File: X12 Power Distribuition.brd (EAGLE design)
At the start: 152.4 x 76.2 mm, 47 parts, among them Q1 SPB80P06P, Y1 ECS-80-S-4X

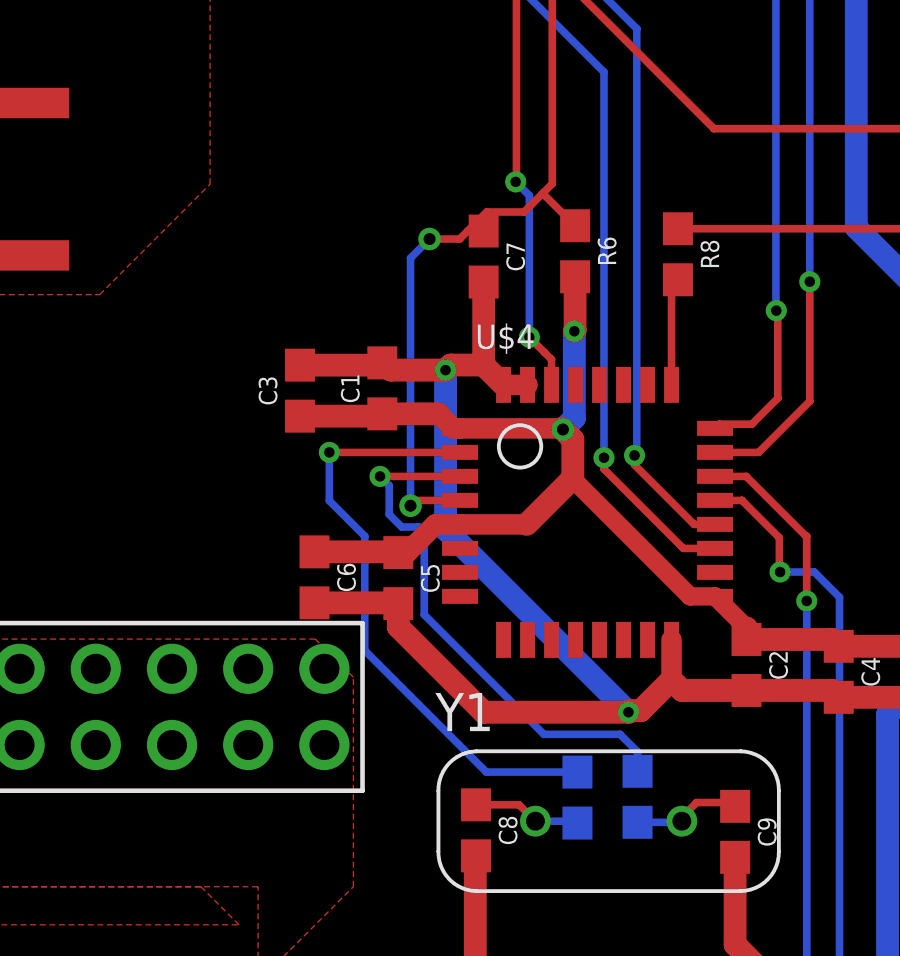
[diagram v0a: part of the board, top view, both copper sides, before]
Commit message: Matched Impedances around crystal
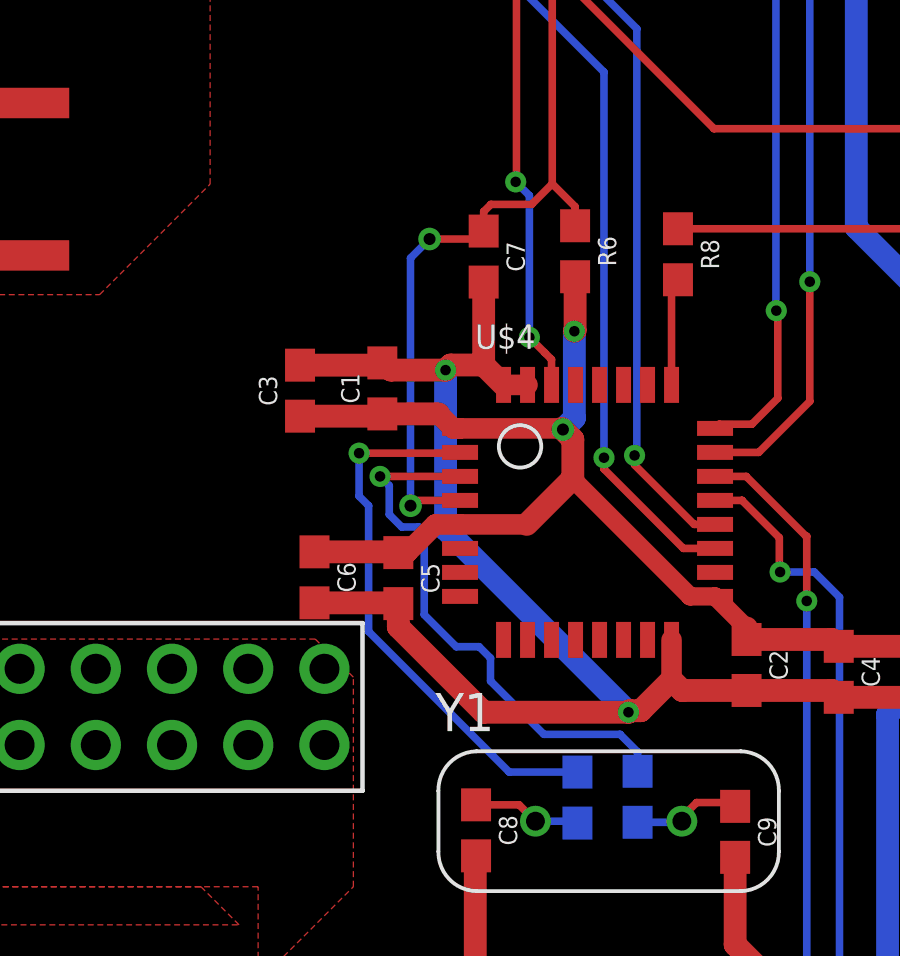
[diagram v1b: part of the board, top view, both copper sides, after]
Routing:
- net OSC_IN: track 20.2 -> 18.4 mm
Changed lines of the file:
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@@
 <wire x1="147.4216" y1="57.652" x2="136.4802" y2="57.652" width="0.254" layer="1"/>
 <wire x1="136.4802" y1="57.652" x2="131.0894" y2="63.0428" width="0.254" layer="1"/>
-<wire x1="131.8514" y1="54.4186" x2="130.7719" y2="55.4981" width="0.254" layer="1"/>
-<wire x1="131.0894" y1="55.8156" x2="130.7719" y2="55.4981" width="0.254" layer="1"/>
-<wire x1="130.1496" y1="54.8758" x2="128.905" y2="54.8758" width="0.254" layer="1"/>
-<wire x1="128.8034" y1="54.2408" x2="128.27" y2="54.2408" width="0.254" layer="1"/>
+<wire x1="131.8514" y1="54.4186" x2="131.8514" y2="55.0536" width="0.254" layer="1"/>
+<wire x1="131.8514" y1="55.0536" x2="131.0894" y2="55.8156" width="0.254" layer="1"/>
 <wire x1="128.016" y1="45.2624" x2="126.5424" y2="45.2624" width="0.254" layer="1"/>
 <wire x1="126.5424" y1="45.2624" x2="126.365" y2="45.085" width="0.254" layer="1"/>
@@
 <wire x1="126.365" y1="53.34" x2="127" y2="53.975" width="0.254" layer="16"/>
 <via x="127" y="53.975" extent="1-16" drill="0.4"/>
-<wire x1="127" y1="53.975" x2="128.0042" y2="53.975" width="0.254" layer="1"/>
-<wire x1="128.27" y1="54.2408" x2="128.905" y2="54.8758" width="0.254" layer="1"/>
-<wire x1="130.7719" y1="55.4981" x2="130.1496" y2="54.8758" width="0.254" layer="1"/>
-<wire x1="128.0042" y1="53.975" x2="128.27" y2="54.2408" width="0.254" layer="1"/>
+<wire x1="130.4036" y1="55.1298" x2="131.0894" y2="55.8156" width="0.254" layer="1"/>
+<wire x1="128.5376" y1="53.975" x2="128.8034" y2="54.2408" width="0.254" layer="1"/>
+<wire x1="127" y1="53.975" x2="128.5376" y2="53.975" width="0.254" layer="1"/>
+<wire x1="128.8034" y1="54.2408" x2="128.8034" y2="54.8894" width="0.254" layer="1"/>
+<wire x1="129.0438" y1="55.1298" x2="130.4036" y2="55.1298" width="0.254" layer="1"/>
+<wire x1="128.8034" y1="54.8894" x2="129.0438" y2="55.1298" width="0.254" layer="1"/>
 </signal>
 <signal name="SWDIO">
@@
 <contactref element="U$4" pad="PF0-OSC_IN"/>
 <contactref element="R7" pad="2"/>
-<wire x1="128.016" y1="46.8624" x2="123.6602" y2="46.8624" width="0.254" layer="1"/>
-<via x="123.6602" y="46.8624" extent="1-16" drill="0.35"/>
-<wire x1="131.9276" y1="36.2068" x2="128.8932" y2="36.2068" width="0.254" layer="16"/>
-<wire x1="123.6602" y1="45.2498" x2="123.6602" y2="46.8624" width="0.254" layer="16"/>
-<wire x1="128.8932" y1="36.2068" x2="124.841" y2="40.259" width="0.254" layer="16"/>
-<wire x1="124.841" y1="40.259" x2="124.841" y2="44.069" width="0.254" layer="16"/>
-<wire x1="124.841" y1="44.069" x2="123.6602" y2="45.2498" width="0.254" layer="16"/>
+<wire x1="128.016" y1="46.8624" x2="127.9906" y2="46.837" width="0.254" layer="1"/>
+<wire x1="127.9906" y1="46.837" x2="124.6508" y2="46.837" width="0.254" layer="1"/>
+<via x="124.6508" y="46.837" extent="1-16" drill="0.35"/>
+<wire x1="131.9276" y1="36.2068" x2="129.6552" y2="36.2068" width="0.254" layer="16"/>
+<wire x1="129.6552" y1="36.2068" x2="124.968" y2="40.894" width="0.254" layer="16"/>
+<wire x1="124.968" y1="40.894" x2="124.968" y2="45.085" width="0.254" layer="16"/>
+<wire x1="124.968" y1="45.085" x2="124.6508" y2="45.4022" width="0.254" layer="16"/>
+<wire x1="124.6508" y1="46.837" x2="124.6508" y2="45.4022" width="0.254" layer="16"/>
 </signal>
 <signal name="OSC_OUT">
@@
 <wire x1="125.657" y1="44.79173125" x2="125.657" y2="45.7548" width="0.254" layer="16"/>
 <wire x1="133.35" y1="37.465" x2="130.81" y2="37.465" width="0.254" layer="16"/>
-<wire x1="130.81" y1="37.465" x2="126.8222" y2="41.4528" width="0.254" layer="16"/>
 <wire x1="126.8222" y1="41.4528" x2="126.8222" y2="44.196" width="0.254" layer="16"/>
+<wire x1="129.032" y1="39.243" x2="129.032" y2="40.005" width="0.254" layer="16"/>
+<wire x1="129.032" y1="40.005" x2="128.651" y2="40.386" width="0.254" layer="16"/>
+<wire x1="127.889" y1="40.386" x2="126.8222" y2="41.4528" width="0.254" layer="16"/>
+<wire x1="130.81" y1="37.465" x2="129.032" y2="39.243" width="0.254" layer="16"/>
+<wire x1="128.651" y1="40.386" x2="127.889" y2="40.386" width="0.254" layer="16"/>
 </signal>
 <signal name="N$6">

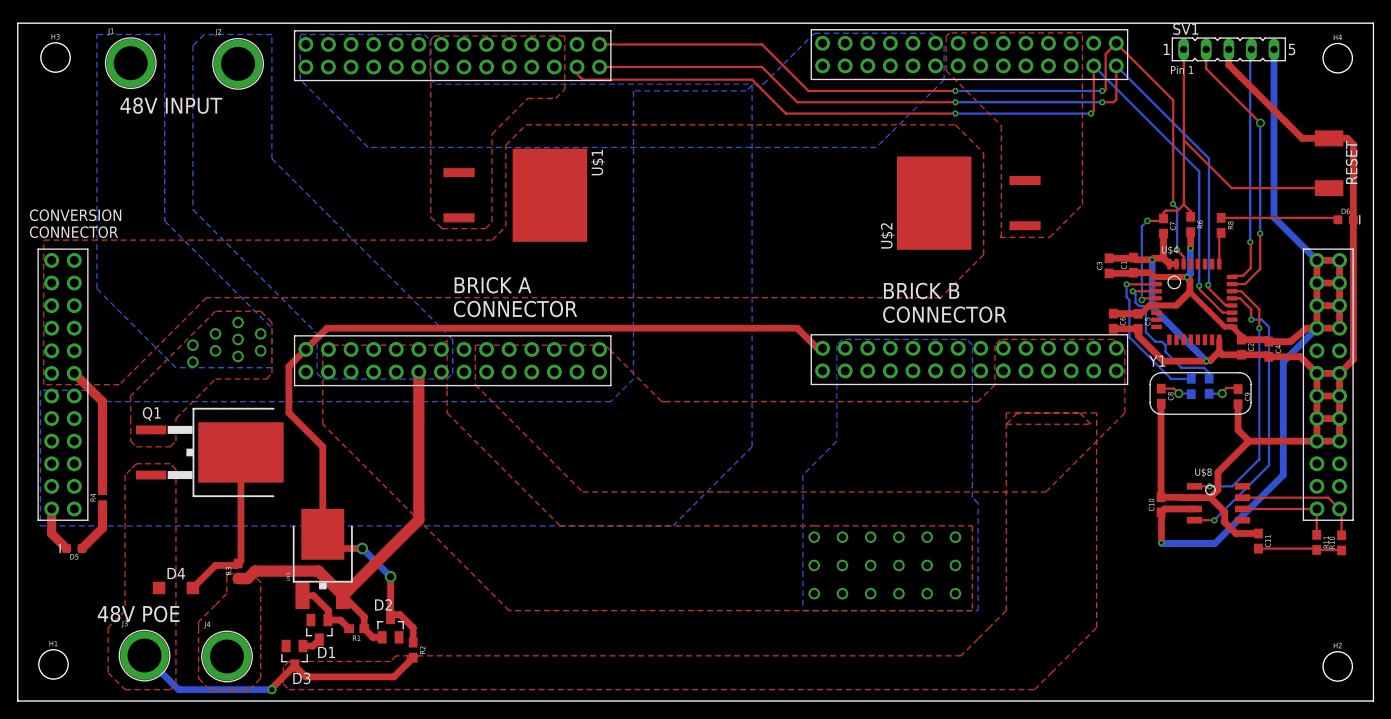
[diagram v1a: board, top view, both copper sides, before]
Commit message: Moved Crystal. Small Fixes
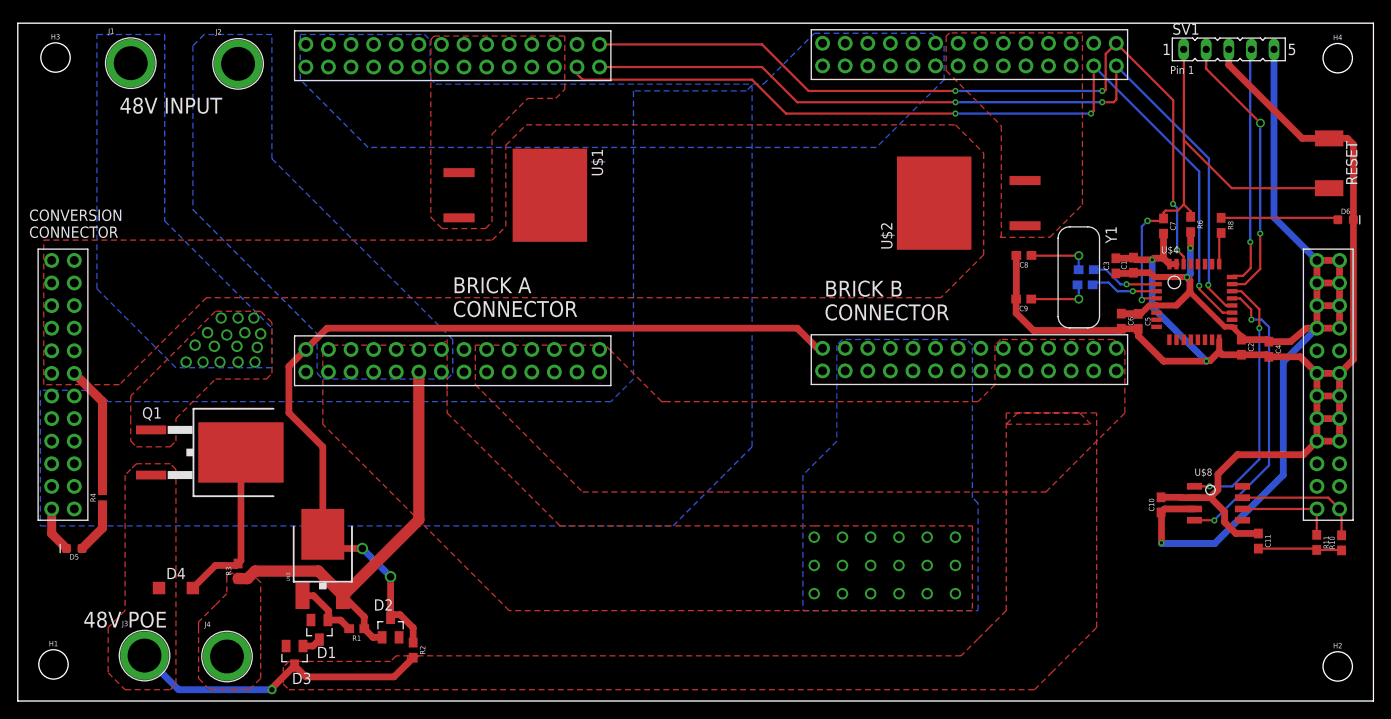
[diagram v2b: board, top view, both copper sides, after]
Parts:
- moved C9 26.5 mm to (113.1, 45.2), turned to 180 degrees
- moved C8 22.1 mm to (113.1, 50.1), turned to 180 degrees
- moved Y1 18.9 mm to (119.3, 47.6), turned to 270 degrees
- moved R5 18.0 mm to (120.0, 46.8), turned to 180 degrees
- moved R7 17.7 mm to (120.1, 48.5), turned to 180 degrees
- moved C6 0.89 mm to (124.1, 42.7)
- moved C3 0.76 mm to (123.4, 48.9)
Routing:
- net OSC_OUT: track 18.3 -> 7.69 mm
- net OSC_IN: track 18.4 -> 7.74 mm
- net N$6: track 3.65 -> 7.01 mm
- net N$7: track 3.63 -> 6.91 mm
- net 3V3GND: track 167.9 -> 170.2 mm
- net +3V3: track 136.6 -> 134.9 mm
